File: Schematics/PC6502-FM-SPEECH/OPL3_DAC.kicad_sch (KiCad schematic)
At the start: 20 parts, among them U2 MCP6002-xSN, U3 MCP6002-xSN, U4 YMF262-M, U7 YAC512-M, X1 CXO_DIP8

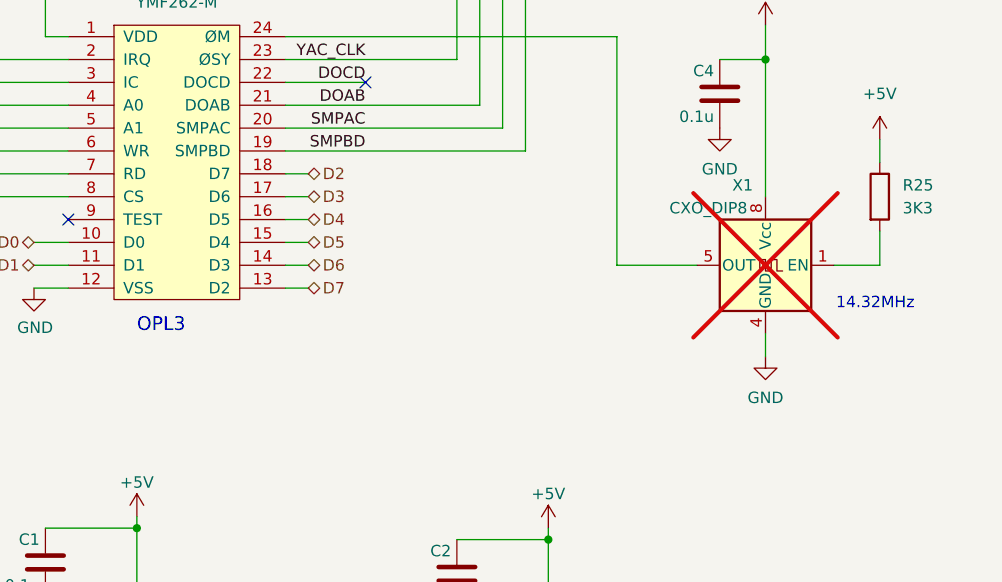
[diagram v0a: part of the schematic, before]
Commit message: Updated Schematics and CPLD files
Files updated for the CPU & FM Speech board
Also revised CPLDs for CPU, VIA and Compact Flasg
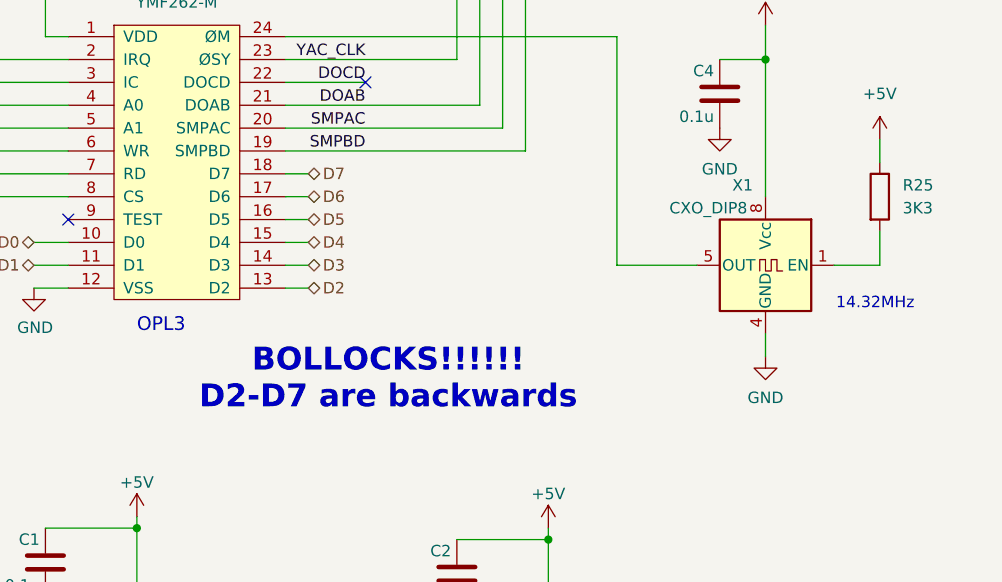
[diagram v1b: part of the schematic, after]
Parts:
- X1: now fitted
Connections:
- net D2: now also U4.13 (D2); no longer U4.18 (D7)
- net D3: now also U4.14 (D3); no longer U4.17 (D6)
- net D4: now also U4.15 (D4); no longer U4.16 (D5)
- net D5: now also U4.16 (D5); no longer U4.15 (D4)
- net D6: now also U4.17 (D6); no longer U4.14 (D3)
- net D7: now also U4.18 (D7); no longer U4.13 (D2)
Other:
- note added: "BOLLOCKS!!!!!! D2-D7 are backwards"
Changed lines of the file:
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@@
 		)
 	)
+	(text "BOLLOCKS!!!!!!\nD2-D7 are backwards "
+		(exclude_from_sim no)
+		(at 111.76 139.7 0)
+		(effects
+			(font
+				(size 2.54 2.54)
+				(thickness 0.508)
+				(bold yes)
+				(color 255 0 35 1)
+			)
+		)
+	)
 	(text "14.32MHz"
 		(exclude_from_sim no)
@@
 	(wire
 		(pts
-			(xy 100.33 116.84) (xy 102.87 116.84)
+			(xy 100.33 129.54) (xy 102.87 129.54)
 		)
 		(stroke
@@
 	(wire
 		(pts
-			(xy 100.33 127) (xy 102.87 127)
+			(xy 100.33 119.38) (xy 102.87 119.38)
 		)
 		(stroke
@@
 	(wire
 		(pts
-			(xy 100.33 124.46) (xy 102.87 124.46)
+			(xy 100.33 121.92) (xy 102.87 121.92)
 		)
 		(stroke
@@
 	(wire
 		(pts
-			(xy 100.33 119.38) (xy 102.87 119.38)
+			(xy 100.33 127) (xy 102.87 127)
 		)
 		(stroke
@@
 	(wire
 		(pts
-			(xy 100.33 121.92) (xy 102.87 121.92)
+			(xy 100.33 124.46) (xy 102.87 124.46)
 		)
 		(stroke
@@
 	(wire
 		(pts
-			(xy 100.33 129.54) (xy 102.87 129.54)
+			(xy 100.33 116.84) (xy 102.87 116.84)
 		)
 		(stroke
@@
 	(hierarchical_label "D5"
 		(shape bidirectional)
-		(at 102.87 124.46 0)
+		(at 102.87 121.92 0)
 		(effects
 			(font
@@
 	(hierarchical_label "D2"
 		(shape bidirectional)
-		(at 102.87 116.84 0)
+		(at 102.87 129.54 0)
 		(effects
 			(font
@@
 	(hierarchical_label "D3"
 		(shape bidirectional)
-		(at 102.87 119.38 0)
+		(at 102.87 127 0)
 		(effects
 			(font
@@
 	(hierarchical_label "D6"
 		(shape bidirectional)
-		(at 102.87 127 0)
+		(at 102.87 119.38 0)
 		(effects
 			(font
@@
 	(hierarchical_label "D4"
 		(shape bidirectional)
-		(at 102.87 121.92 0)
+		(at 102.87 124.46 0)
 		(effects
 			(font
@@
 	(hierarchical_label "D7"
 		(shape bidirectional)
-		(at 102.87 129.54 0)
+		(at 102.87 116.84 0)
 		(effects
 			(font
@@
 		(in_bom yes)
 		(on_board yes)
-		(dnp yes)
+		(dnp no)
 		(property "Reference" "X1"
 			(at 151.13 118.11 0)
